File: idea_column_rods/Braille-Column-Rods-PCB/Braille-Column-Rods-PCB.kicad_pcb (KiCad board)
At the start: 2 copper layers, 95 x 99 mm, 155 parts, among them J1 Conn_01x03, J3 Conn_01x02, J4 Conn_01x08, J5 Screw_Terminal_01x02, J6 Screw_Terminal_01x02, J7 Conn_01x02, M1 Stepper_Motor_bipolar, M10 Motor_DC_With_MP, M11 Motor_DC_With_MP, M12 Motor_DC_With_MP, M2 Stepper_Motor_bipolar, M3 Stepper_Motor_bipolar, M4 Stepper_Motor_bipolar, M5 Stepper_Motor_bipolar, M6 Stepper_Motor_bipolar, M7 Stepper_Motor_bipolar, M8 Stepper_Motor_bipolar, M9 Motor_DC_With_MP, SW1 SW_Push, SW2 SW_Push, U1 DRV8847SPWR, U10 AD116, U11 AD116, U12 AD116, U13 AD116, U14 74HC595, U15 74HC595, U17 MT910xET, U18 MT910xET, U19 MT910xET, U2 DRV8847SPWR, U20 MT910xET, U21 MT910xET, U22 MT910xET, U23 MT910xET, U24 MT910xET, U25 MT910xET, U26 MT910xET, U27 MT910xET, U28 MT910xET, U3 RP2040-Zero, U30 CD74HC4067M, U4 DRV8847SPWR, U5 DRV8847SPWR, U6 DRV8847SPWR, U7 DRV8847SPWR, U8 DRV8847SPWR, U9 DRV8847SPWR

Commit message: Big routing
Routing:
- net GND: track 0.00 -> 688.4 mm, vias 0 -> 90
- net +3V3: track 33.8 -> 416.2 mm, vias 8 -> 13
- net VDC: track 49.9 -> 310.0 mm, vias 0 -> 5
- net I2C_SCL: track 4.25 -> 250.0 mm, vias 0 -> 15
- net I2C_SDA: track 5.10 -> 159.7 mm, vias 0 -> 4
- net /Motor_Control/HALL_10: track 2.01 -> 103.6 mm, vias 0 -> 2
- net /Motor_Control/HALL_11: track 2.01 -> 77.5 mm
- net /Motor_Control/Braille_Cell_Column3/~{SLEEP}: track 0.00 -> 74.4 mm, vias 0 -> 2
- net /Motor_Control/Braille_Cell_Column1/~{SLEEP}: track 0.00 -> 70.2 mm, vias 0 -> 2
- net /Motor_Control/Braille_Cell_Column2/~{SLEEP}: track 0.00 -> 67.5 mm, vias 0 -> 2
- net /Motor_Control/HALL_8: track 2.01 -> 62.5 mm, vias 0 -> 2
- net /Motor_Control/Braille_Cell_Column/~{SLEEP}: track 0.00 -> 59.2 mm, vias 0 -> 2
- net /Motor_Control/Corner_DC_Motor/IN_A: track 5.24 -> 62.6 mm, vias 0 -> 2
- net /Motor_Control/HALL_1: track 0.00 -> 56.5 mm, vias 1 -> 3
- net /Motor_Control/HALL_3: track 0.00 -> 54.5 mm, vias 1 -> 3
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
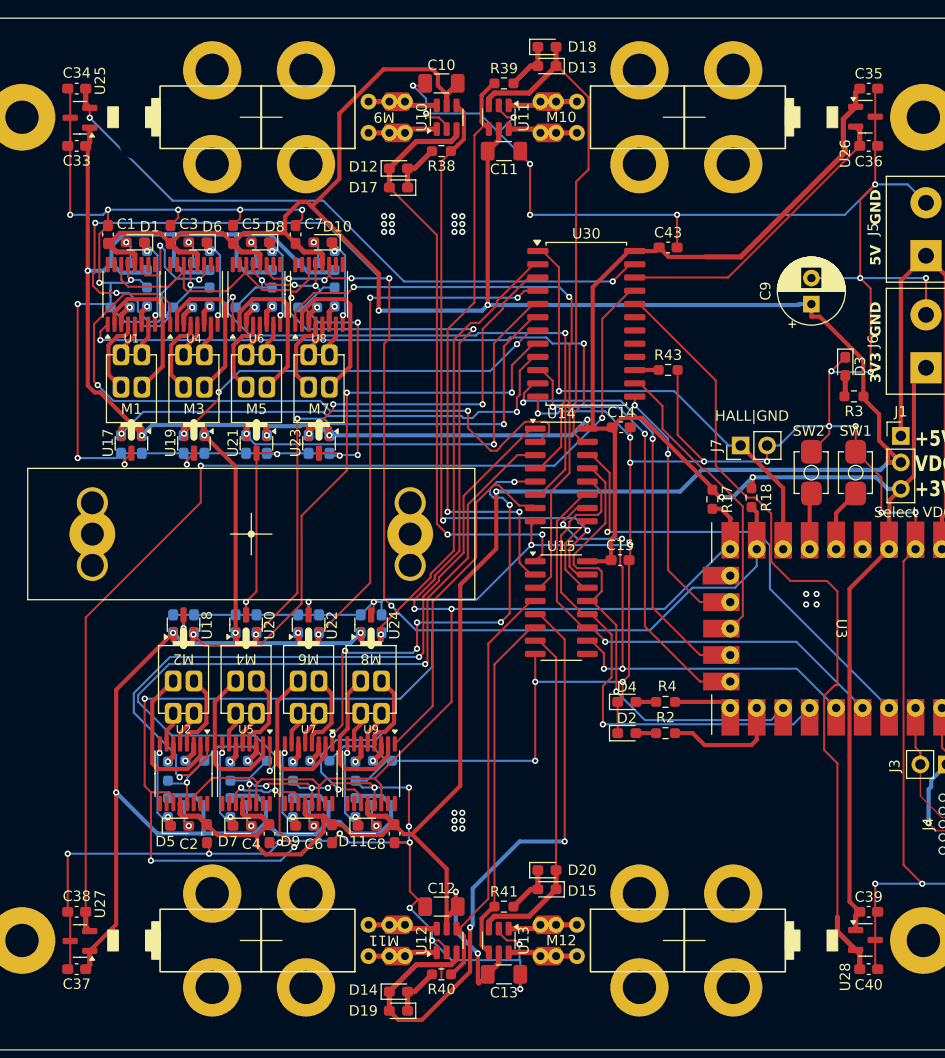
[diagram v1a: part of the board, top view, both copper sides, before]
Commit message: Clean up DRC (mostly footprints)
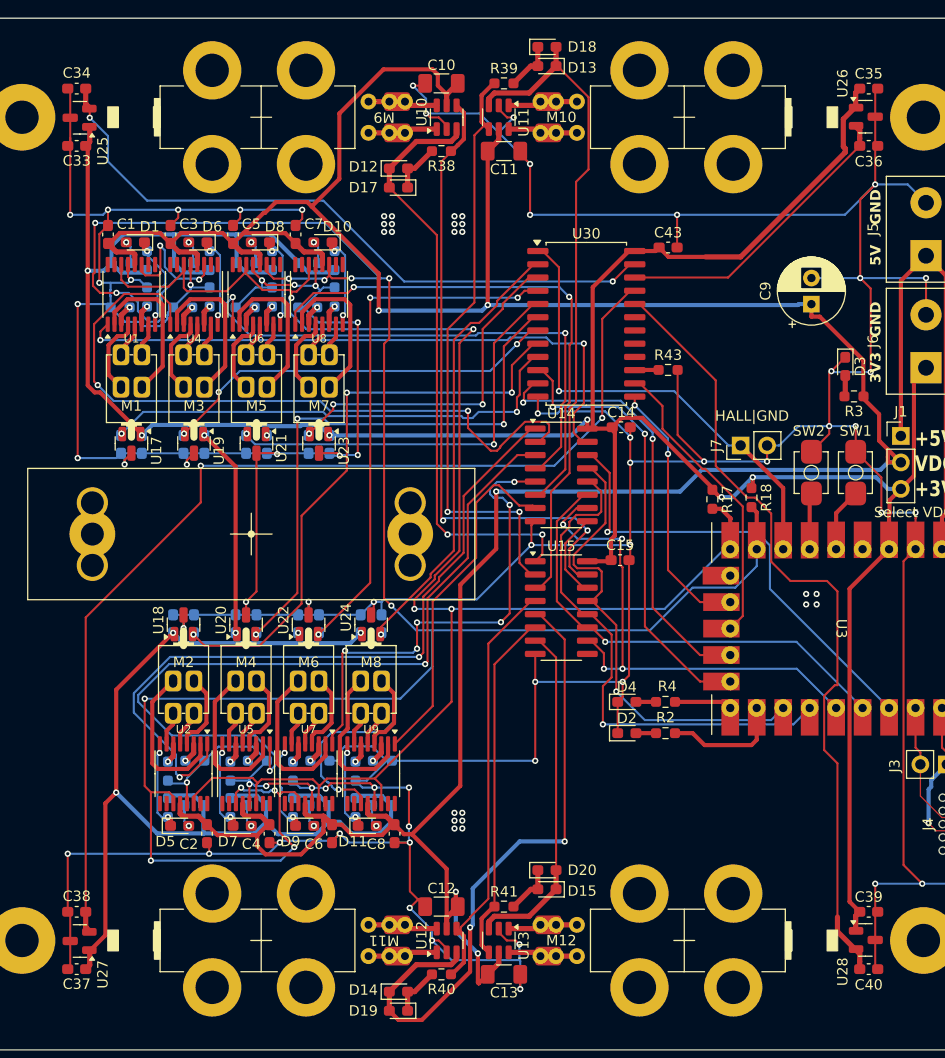
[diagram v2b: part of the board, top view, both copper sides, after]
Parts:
- U17, U18, U19, U20, U21, U22, U23, U24, U25, U26, U27, U28: footprint Package_TO_SOT_SMD:SOT-23 -> 00-lib-footprints:SOT-23-Hall
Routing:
- net VDC: track 310.0 -> 313.1 mm
- net /Motor_Control/HALL_8: track 62.5 -> 63.9 mm
- net /Motor_Control/Corner_DC_Motor2/IN_B: track 63.6 -> 62.3 mm
- net I2C_SCL: track 250.0 -> 251.0 mm
- net /Motor_Control/Braille_Cell_Column5/~{SLEEP}: vias 7 -> 6

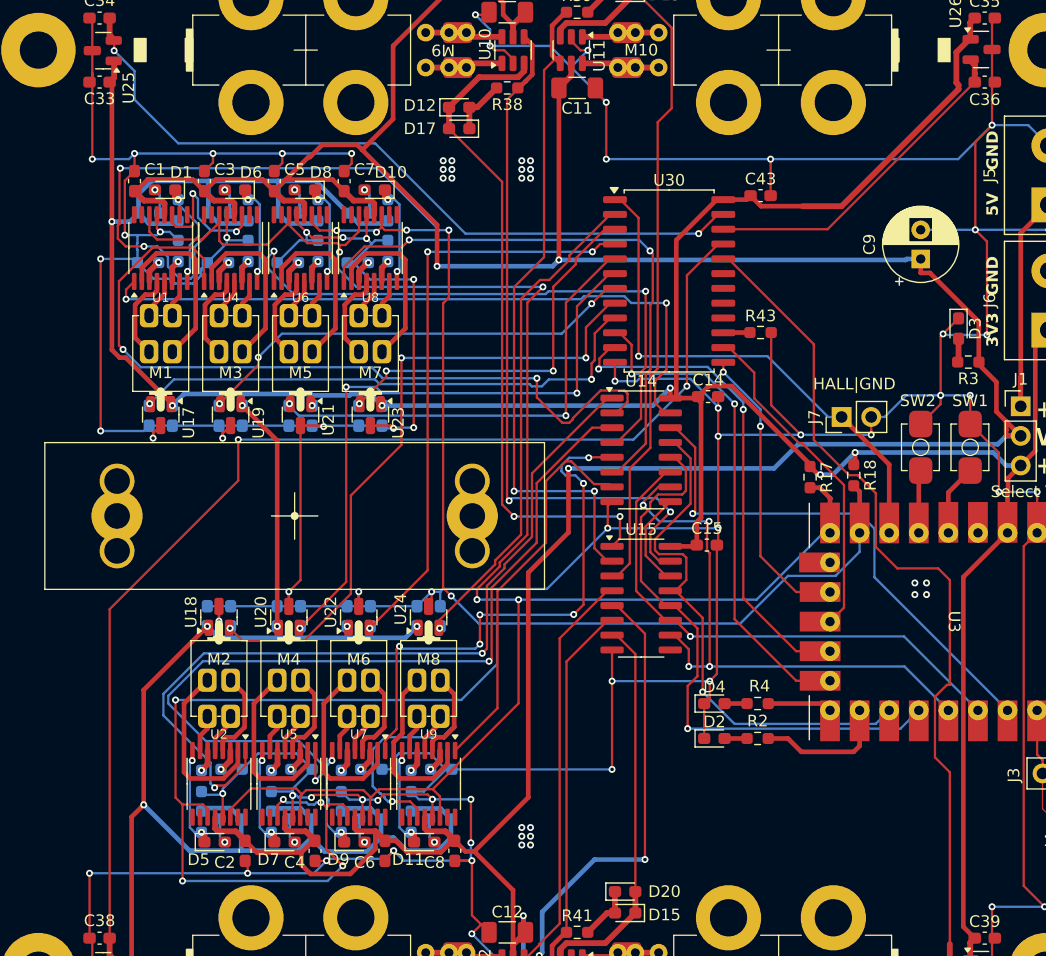
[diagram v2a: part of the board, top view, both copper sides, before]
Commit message: Fix spacing issue on top
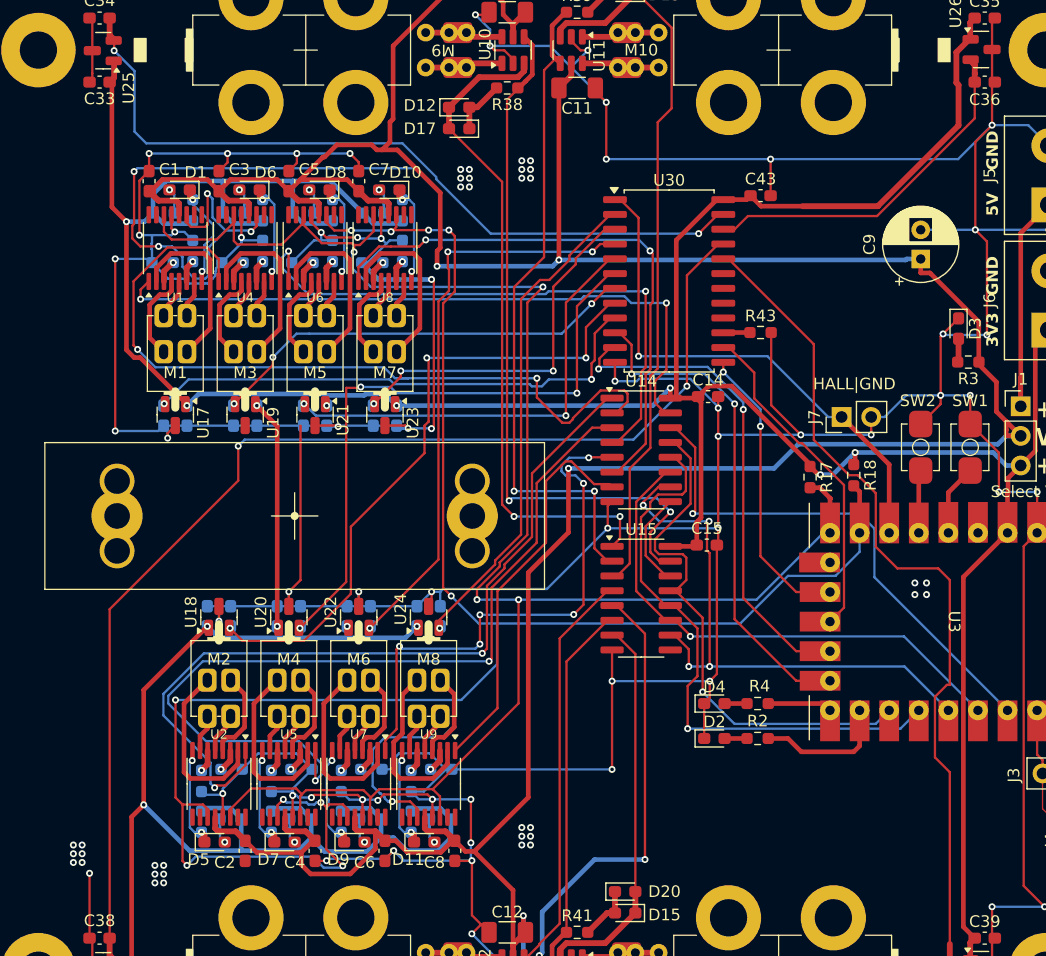
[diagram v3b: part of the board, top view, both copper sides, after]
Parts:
- moved C1 1.25 mm to (97.8, 96.2)
- moved C17 1.25 mm to (101.0, 116.4)
- moved C19 1.25 mm to (107.0, 116.4)
- moved C21 1.25 mm to (113.0, 116.4)
- moved C23 1.25 mm to (119.0, 116.4)
- moved C25 1.25 mm to (99.0, 116.4)
- moved C27 1.25 mm to (105.0, 116.4)
- moved C29 1.25 mm to (111.0, 116.4)
- moved C3 1.25 mm to (103.8, 96.2)
- moved C31 1.25 mm to (117.0, 116.4)
- moved C5 1.25 mm to (109.8, 96.2)
- moved C7 1.25 mm to (115.8, 96.2)
- moved D1 1.25 mm to (100.4, 97.0)
- moved D10 1.25 mm to (118.4, 97.0)
- moved D6 1.25 mm to (106.4, 97.0)
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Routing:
- net GND: track 688.8 -> 654.7 mm, vias 90 -> 99
- net /Motor_Control/HALL_9: track 29.6 -> 31.4 mm
- net /Motor_Control/HALL_8: track 63.9 -> 65.6 mm
- net I2C_SCL: track 251.0 -> 249.7 mm
- net I2C_SDA: track 159.7 -> 158.5 mm
- net /Motor_Control/HALL_6: track 33.2 -> 31.9 mm
- net /Motor_Control/HALL_2: track 38.6 -> 37.4 mm
- net /Motor_Control/HALL_0: track 45.8 -> 44.6 mm
- net /Motor_Control/Braille_Cell_Column4/~{SLEEP}: track 52.2 -> 50.9 mm
- net /Motor_Control/Braille_Cell_Column/~{SLEEP}: track 59.2 -> 57.9 mm
- net /Motor_Control/Braille_Cell_Column6/~{SLEEP}: track 49.7 -> 48.4 mm
- net /Motor_Control/HALL_4: track 39.8 -> 38.6 mm
- net /Motor_Control/HALL_1: track 56.5 -> 55.4 mm
- net /Motor_Control/HALL_5: track 50.9 -> 50.0 mm
- net +3V3: track 416.2 -> 416.8 mm

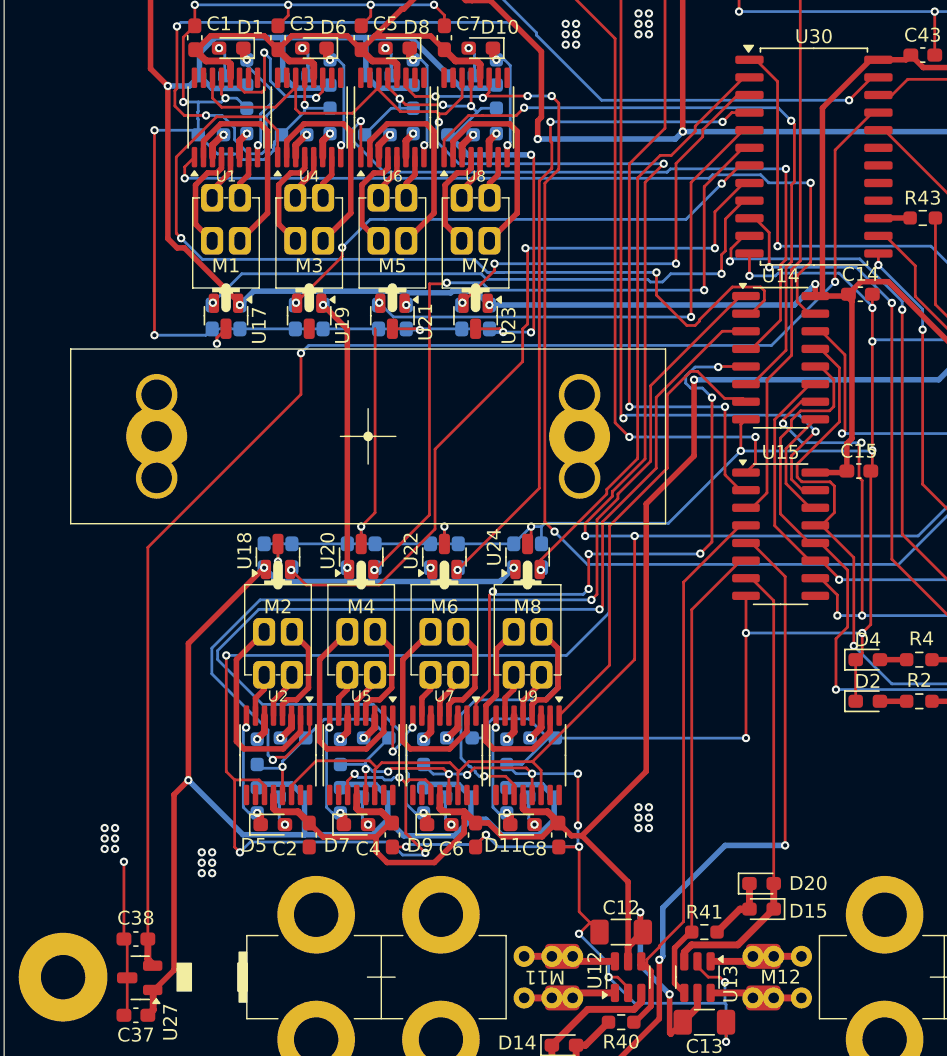
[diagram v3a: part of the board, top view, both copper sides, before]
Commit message: Fix spacing issues on bottom
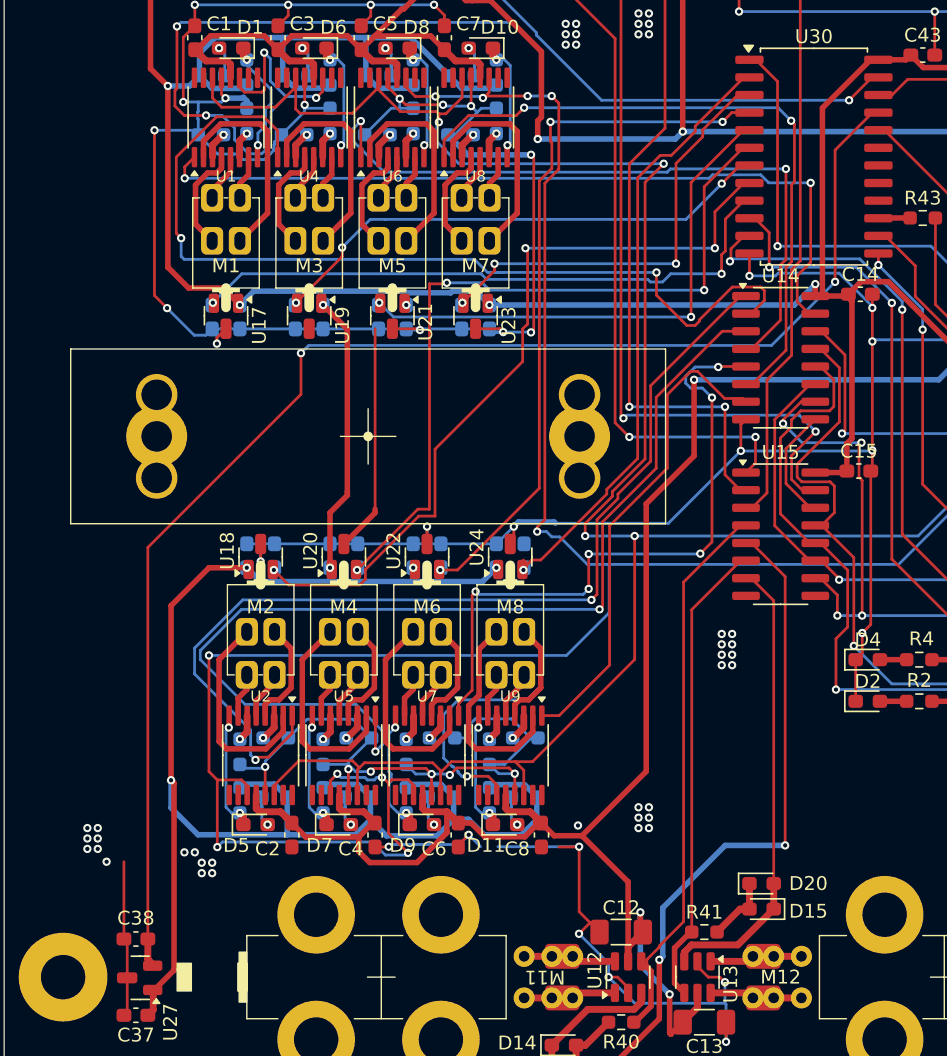
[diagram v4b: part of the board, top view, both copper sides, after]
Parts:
- moved C18 1.25 mm to (101.5, 133.6)
- moved C2 1.25 mm to (104.8, 153.8)
- moved C20 1.25 mm to (107.5, 133.6)
- moved C22 1.25 mm to (113.5, 133.6)
- moved C24 1.25 mm to (119.5, 133.6)
- moved C26 1.25 mm to (103.5, 133.6)
- moved C28 1.25 mm to (109.5, 133.6)
- moved C30 1.25 mm to (115.5, 133.6)
- moved C32 1.25 mm to (121.5, 133.6)
- moved C4 1.25 mm to (110.8, 153.8)
- moved C6 1.25 mm to (116.8, 153.8)
- moved C8 1.25 mm to (122.8, 153.8)
- moved D11 1.25 mm to (120.1, 153.0)
- moved D5 1.25 mm to (102.1, 153.0)
- moved D7 1.25 mm to (108.1, 153.0)
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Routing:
- net GND: track 654.7 -> 612.9 mm, vias 99 -> 103
- net +3V3: track 416.8 -> 420.9 mm
- net I2C_SCL: track 249.7 -> 251.8 mm
- net /Motor_Control/HALL_7: track 42.6 -> 44.3 mm
- net /Motor_Control/HALL_5: track 50.0 -> 51.2 mm
- net VDC: track 313.1 -> 314.4 mm
- net I2C_SDA: track 158.5 -> 159.7 mm
- net /Motor_Control/Braille_Cell_Column7/~{SLEEP}: track 33.7 -> 34.9 mm
- net /Motor_Control/Braille_Cell_Column3/~{SLEEP}: track 74.4 -> 75.7 mm
- net /Motor_Control/Braille_Cell_Column1/~{SLEEP}: track 70.2 -> 71.4 mm
- net /Motor_Control/Braille_Cell_Column5/~{SLEEP}: track 46.2 -> 47.5 mm
- net /Motor_Control/HALL_1: track 55.4 -> 56.5 mm
- net /Motor_Control/HALL_3: track 54.4 -> 55.4 mm
- net /Motor_Control/Braille_Cell_Column2/~{SLEEP}: track 67.2 -> 67.9 mm

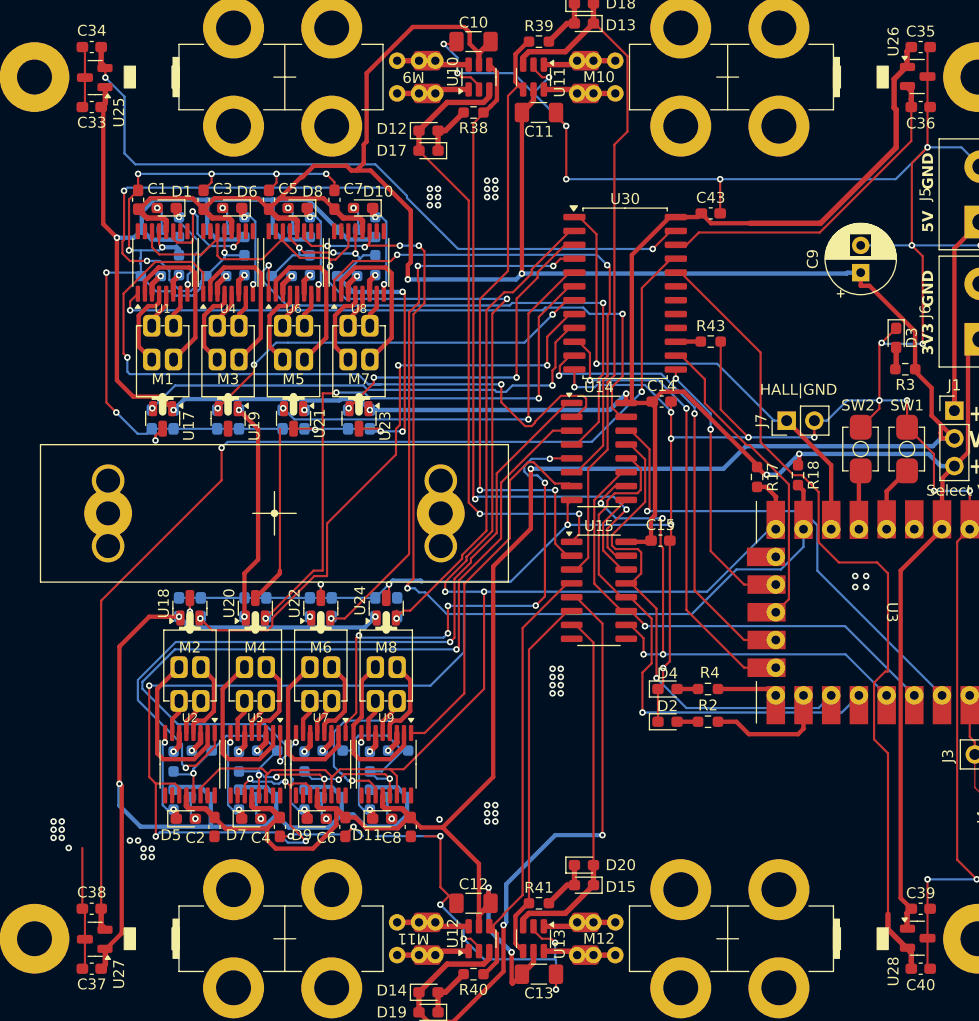
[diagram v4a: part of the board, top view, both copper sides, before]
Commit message: Create render of 6mm motor, add to PCB
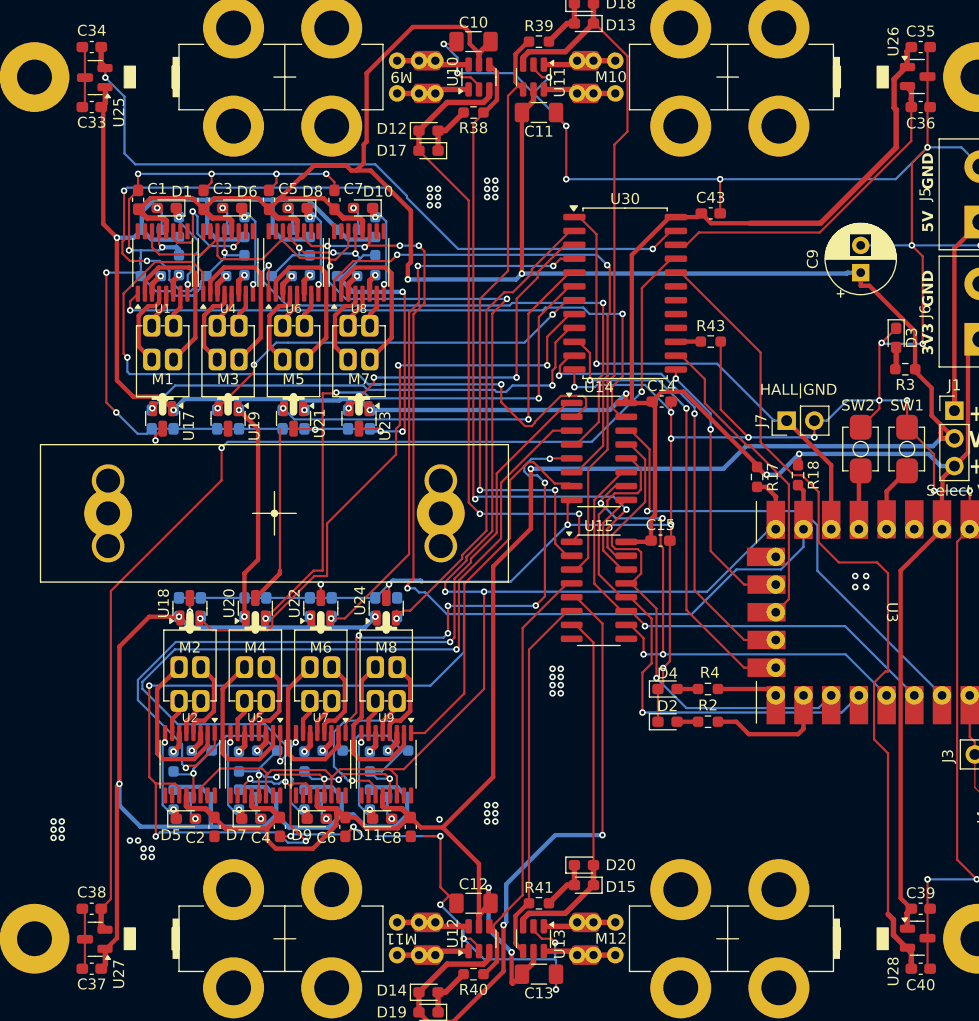
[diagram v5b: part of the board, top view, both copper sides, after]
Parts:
- moved M10 1.10 mm to (162.6, 85.0)
- moved M11 1.10 mm to (100.4, 164.0)
- moved M12 1.10 mm to (162.6, 164.0)
- moved M9 1.10 mm to (100.4, 85.0)
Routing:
- net GND: track 612.9 -> 607.3 mm, vias 103 -> 102

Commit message: WIP: Get cams good
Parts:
- removed H5, H6, H7, H8: MountingHole_Pad, 00-lib-footprints:MountingHole_3.2mm_M3_Pad_NoSilk
- C33, C34: moved to B.Cu
- moved C33 3.01 mm to (95.8, 85.8)
- moved C34 2.93 mm to (95.6, 84.2)
- moved U25 1.69 mm to (95.5, 85.0)
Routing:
- net /Motor_Control/HALL_8: track 65.6 -> 64.0 mm
- net /Motor_Control/Braille_Cell_Column2/~{SLEEP}: track 67.9 -> 67.0 mm
- net GND: track 607.3 -> 606.4 mm, vias 102 -> 105
- net /Motor_Control/HALL_7: track 44.3 -> 43.5 mm
- net +3V3: track 420.7 -> 420.3 mm, vias 13 -> 14
